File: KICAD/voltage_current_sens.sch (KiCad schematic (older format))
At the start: 14 parts, among them U10 LT6016, U11 AD8030

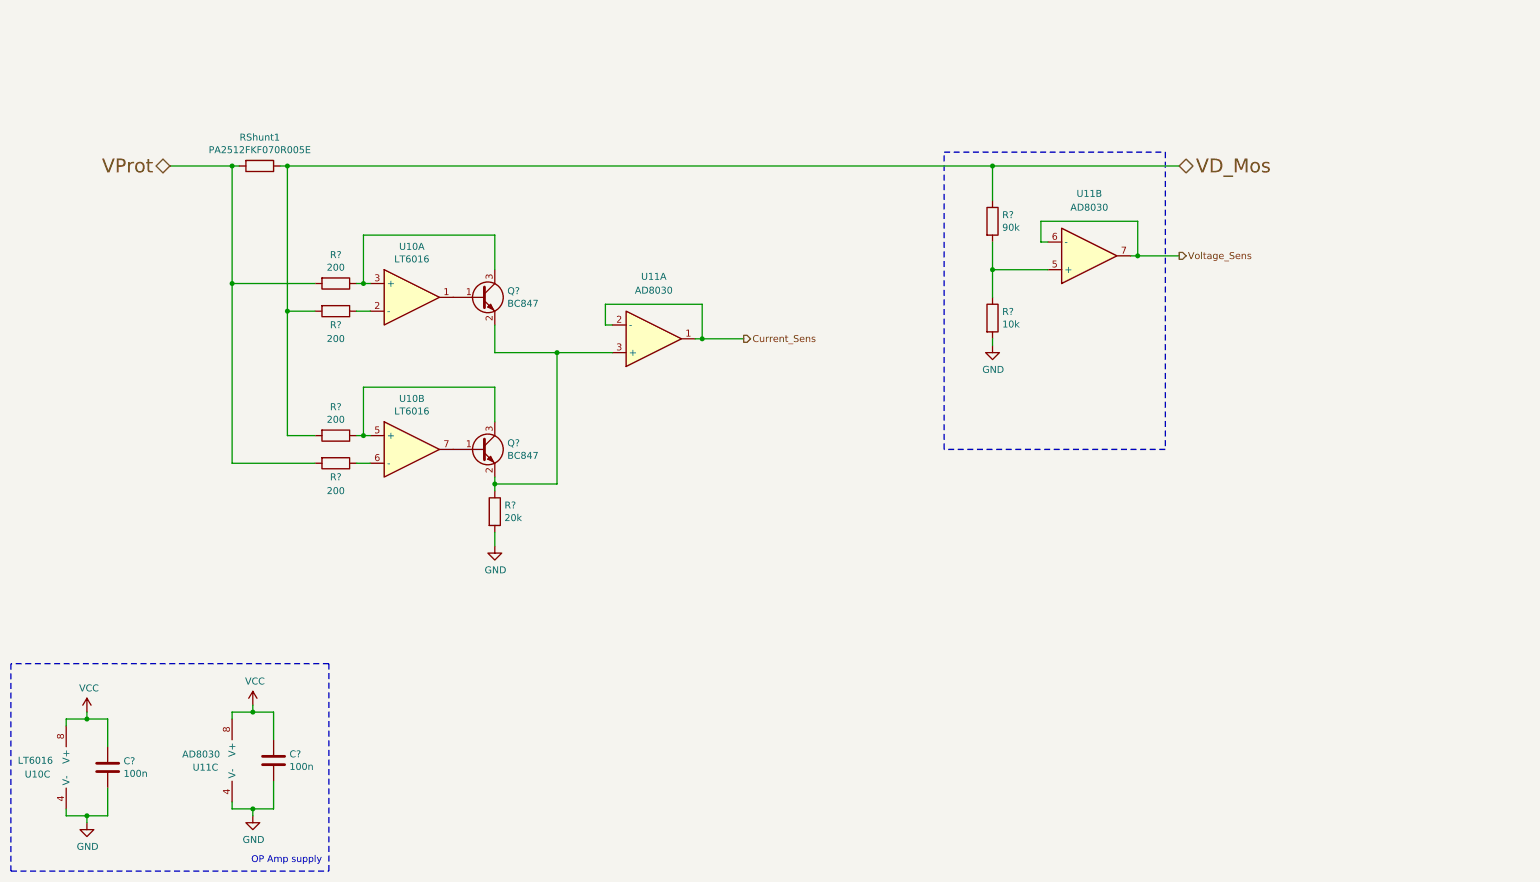
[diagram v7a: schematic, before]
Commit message: drivers draft + clean and minors changes
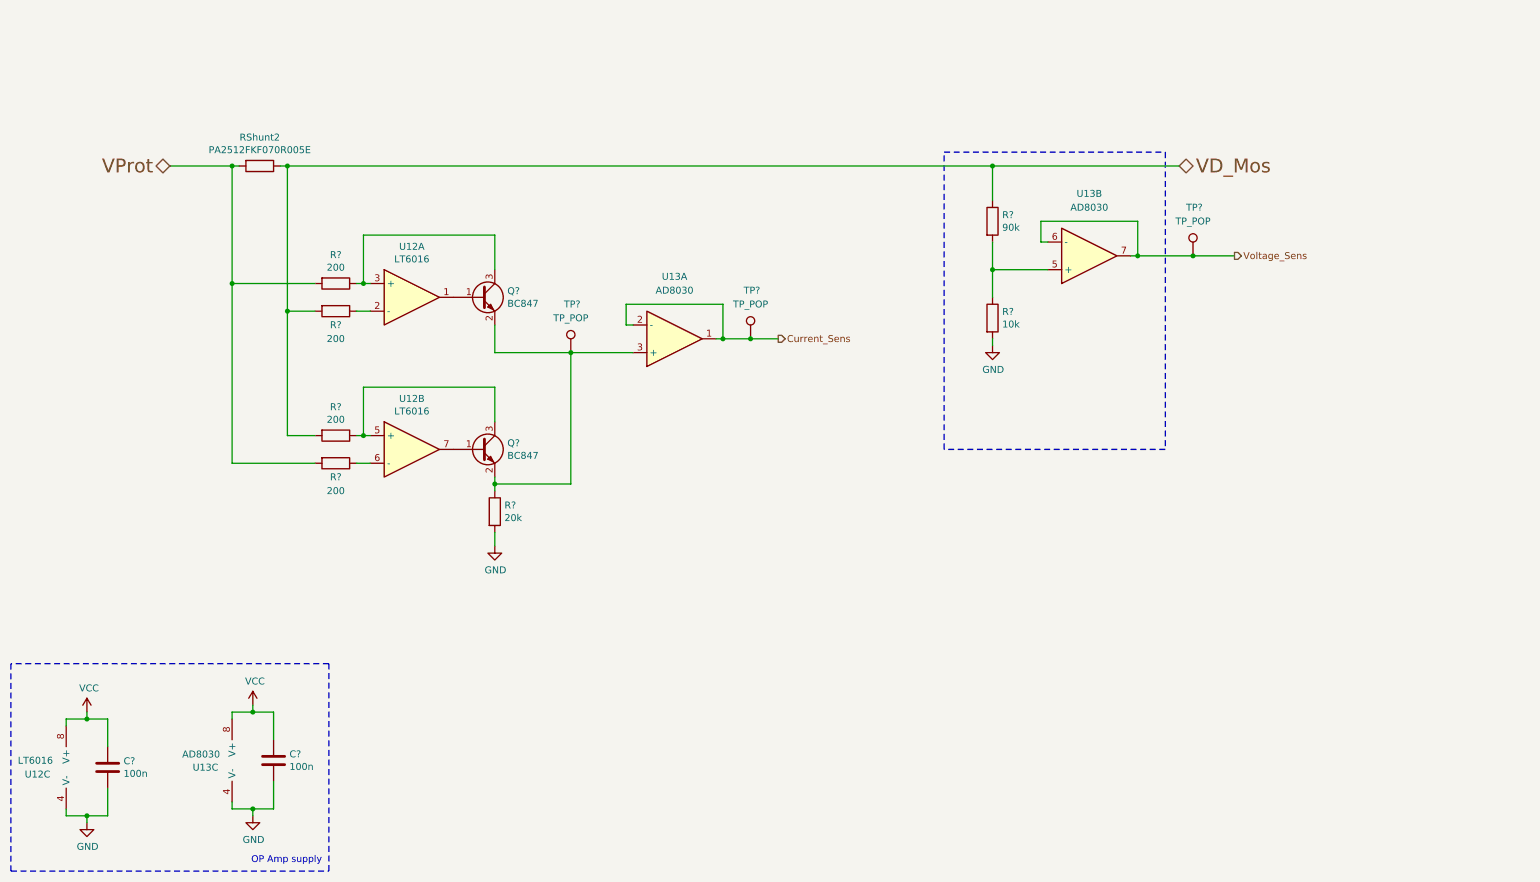
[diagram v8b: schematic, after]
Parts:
- added TP? (x3): TP_POP, symbol Connector:TestPoint
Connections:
- net Current_Sens: now also TP?.1
- net Voltage_Sens: now also TP?.1
- net at Q?.2 (E), Q?.2 (E), R?.1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: now also TP?.1
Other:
- moved on the sheet: U13A
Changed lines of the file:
@@
 $Descr A4 11693 8268
 encoding utf-8
-Sheet 8 16
+Sheet 11 16
 Title "SESAME"
 Date ""
@@
 AR Path="/60F19D5B/6109114F" Ref="RShunt2"  Part="1"
 AR Path="/60F171CE/6109114F" Ref="RShunt1"  Part="1"
-F 0 "RShunt1" V 2143 2600 50  0000 C CNN
+F 0 "RShunt2" V 2143 2600 50  0000 C CNN
 F 1 "PA2512FKF070R005E" V 2234 2600 50  0000 C CNN
 F 2 "Resistor_SMD:R_2512_6332Metric_Pad1.40x3.35mm_HandSolder" V 2280 2600 50  0001 C CNN
@@
 AR Path="/60F171CE/610DEA27" Ref="#PWR0157"  Part="1"
 AR Path="/60F19D5B/610DEA27" Ref="#PWR0112"  Part="1"
-F 0 "#PWR0157" H 7650 3650 50  0001 C CNN
+F 0 "#PWR0112" H 7650 3650 50  0001 C CNN
 F 1 "GND" H 7655 3727 50  0000 C CNN
 F 2 "" H 7650 3900 50  0001 C CNN
@@
 	1    0    0    -1
 $EndComp
-Text HLabel 9000 3250 2    50   Output ~ 0
+Text HLabel 9400 3250 2    50   Output ~ 0
 Voltage_Sens
 Text HLabel 9000 2600 2    100  BiDi ~ 0
@@
 	7650 3350 7650 3550
 Wire Wire Line
-	9000 3250 8700 3250
+	9400 3250 9100 3250
 Connection ~ 8700 3250
 Wire Wire Line
@@
 	4050 4850 4050 4900
 Wire Wire Line
-	4050 4900 4500 4900
-Wire Wire Line
-	4500 4900 4500 3950
-Wire Wire Line
-	4500 3950 4050 3950
+	4050 4900 4600 4900
+Wire Wire Line
+	4600 4900 4600 3950
+Wire Wire Line
+	4600 3950 4050 3950
 Wire Wire Line
 	4050 3950 4050 3750
@@
 AR Path="/60F171CE/6139E98B" Ref="U11"  Part="2"
 AR Path="/60F19D5B/6139E98B" Ref="U13"  Part="2"
-F 0 "U11" H 8350 2800 50  0000 C CNN
+F 0 "U13" H 8350 2800 50  0000 C CNN
 F 1 "AD8030" H 8350 2900 50  0000 C CNN
 F 2 "Package_SO:SO-8_3.9x4.9mm_P1.27mm" H 8350 3250 50  0001 C CNN
@@
 $EndComp
 Wire Wire Line
-	5500 3850 5550 3850
-Wire Wire Line
-	5550 3600 4850 3600
-Wire Wire Line
-	4850 3600 4850 3750
-Wire Wire Line
-	4850 3750 4900 3750
-Wire Wire Line
-	5550 3600 5550 3850
-Wire Wire Line
-	4900 3950 4500 3950
-Wire Wire Line
-	5850 3850 5550 3850
-Connection ~ 5550 3850
+	5650 3850 5700 3850
+Wire Wire Line
+	5700 3600 5000 3600
+Wire Wire Line
+	5000 3600 5000 3750
+Wire Wire Line
+	5000 3750 5050 3750
+Wire Wire Line
+	5700 3600 5700 3850
+Wire Wire Line
+	5050 3950 4600 3950
+Wire Wire Line
+	6100 3850 5900 3850
+Connection ~ 5700 3850
 $Comp
 L Sesame:AD8030 U11
 U 1 1 613A5251
-P 5200 3850
+P 5350 3850
 AR Path="/60F171CE/613A5251" Ref="U11"  Part="1"
 AR Path="/60F19D5B/613A5251" Ref="U13"  Part="1"
-F 0 "U11" H 5200 3400 50  0000 C CNN
-F 1 "AD8030" H 5200 3500 50  0000 C CNN
-F 2 "Package_SO:SO-8_3.9x4.9mm_P1.27mm" H 5200 3850 50  0001 C CNN
-F 3 "~" H 5200 3850 50  0001 C CNN
-	1    5200 3850
+F 0 "U13" H 5350 3400 50  0000 C CNN
+F 1 "AD8030" H 5350 3500 50  0000 C CNN
+F 2 "Package_SO:SO-8_3.9x4.9mm_P1.27mm" H 5350 3850 50  0001 C CNN
+F 3 "~" H 5350 3850 50  0001 C CNN
+	1    5350 3850
 	1    0    0    1
 $EndComp
-Connection ~ 4500 3950
-Text HLabel 5850 3850 2    50   Output ~ 0
+Connection ~ 4600 3950
+Text HLabel 6100 3850 2    50   Output ~ 0
 Current_Sens
 $Comp
@@
 AR Path="/60F171CE/613B75A3" Ref="U11"  Part="3"
 AR Path="/60F19D5B/613B75A3" Ref="U13"  Part="3"
-F 0 "U11" H 2050 6850 50  0000 R CNN
+F 0 "U13" H 2050 6850 50  0000 R CNN
 F 1 "AD8030" H 2063 6945 50  0000 R CNN
 F 2 "Package_SO:SO-8_3.9x4.9mm_P1.27mm" H 2250 6900 50  0001 C CNN
@@
 AR Path="/60F171CE/615B8C9F" Ref="U10"  Part="1"
 AR Path="/60F19D5B/615B8C9F" Ref="U12"  Part="1"
-F 0 "U10" H 3450 3917 50  0000 C CNN
+F 0 "U12" H 3450 3917 50  0000 C CNN
 F 1 "LT6016" H 3450 3826 50  0000 C CNN
 F 2 "Package_SO:MSOP-8_3x3mm_P0.65mm" H 3450 3550 50  0001 C CNN
@@
 AR Path="/60F171CE/615BC62A" Ref="U10"  Part="2"
 AR Path="/60F19D5B/615BC62A" Ref="U12"  Part="2"
-F 0 "U10" H 3450 5017 50  0000 C CNN
+F 0 "U12" H 3450 5017 50  0000 C CNN
 F 1 "LT6016" H 3450 4926 50  0000 C CNN
 F 2 "Package_SO:MSOP-8_3x3mm_P0.65mm" H 3450 4650 50  0001 C CNN
@@
 AR Path="/60F171CE/615BFCFC" Ref="U10"  Part="3"
 AR Path="/60F19D5B/615BFCFC" Ref="U12"  Part="3"
-F 0 "U10" H 650 6900 50  0000 L CNN
+F 0 "U12" H 650 6900 50  0000 L CNN
 F 1 "LT6016" H 600 7000 50  0000 L CNN
 F 2 "Package_SO:MSOP-8_3x3mm_P0.65mm" H 1050 6950 50  0001 C CNN
@@
 Wire Notes Line
 	550  7700 2850 7700
+$Comp
+L Connector:TestPoint TP?
+U 1 1 6153C862
+P 4600 3950
+AR Path="/614794AE/6153C862" Ref="TP?"  Part="1"
+AR Path="/61456C6A/6153C862" Ref="TP?"  Part="1"
+AR Path="/6153C862" Ref="TP?"  Part="1"
+AR Path="/60F1AA92/6153C862" Ref="TP?"  Part="1"
+AR Path="/60F171CE/6153C862" Ref="TP?"  Part="1"
+AR Path="/60F19D5B/6153C862" Ref="TP?"  Part="1"
+F 0 "TP?" H 4550 4300 50  0000 L CNN
+F 1 "TP_POP" H 4600 4200 50  0000 C CNN
+F 2 "" H 4800 3950 50  0001 C CNN
+F 3 "~" H 4800 3950 50  0001 C CNN
+	1    4600 3950
+	1    0    0    -1
+$EndComp
+$Comp
+L Connector:TestPoint TP?
+U 1 1 61544B27
+P 9100 3250
+AR Path="/614794AE/61544B27" Ref="TP?"  Part="1"
+AR Path="/61456C6A/61544B27" Ref="TP?"  Part="1"
+AR Path="/61544B27" Ref="TP?"  Part="1"
+AR Path="/60F1AA92/61544B27" Ref="TP?"  Part="1"
+AR Path="/60F171CE/61544B27" Ref="TP?"  Part="1"
+AR Path="/60F19D5B/61544B27" Ref="TP?"  Part="1"
+F 0 "TP?" H 9050 3600 50  0000 L CNN
+F 1 "TP_POP" H 9100 3500 50  0000 C CNN
+F 2 "" H 9300 3250 50  0001 C CNN
+F 3 "~" H 9300 3250 50  0001 C CNN
+	1    9100 3250
+	1    0    0    -1
+$EndComp
+Connection ~ 9100 3250
+Wire Wire Line
+	9100 3250 8700 3250
+$Comp
+L Connector:TestPoint TP?
+U 1 1 6154A16C
+P 5900 3850
+AR Path="/614794AE/6154A16C" Ref="TP?"  Part="1"
+AR Path="/61456C6A/6154A16C" Ref="TP?"  Part="1"
+AR Path="/6154A16C" Ref="TP?"  Part="1"
+AR Path="/60F1AA92/6154A16C" Ref="TP?"  Part="1"
+AR Path="/60F171CE/6154A16C" Ref="TP?"  Part="1"
+AR Path="/60F19D5B/6154A16C" Ref="TP?"  Part="1"
+F 0 "TP?" H 5850 4200 50  0000 L CNN
+F 1 "TP_POP" H 5900 4100 50  0000 C CNN
+F 2 "" H 6100 3850 50  0001 C CNN
+F 3 "~" H 6100 3850 50  0001 C CNN
+	1    5900 3850
+	1    0    0    -1
+$EndComp
+Connection ~ 5900 3850
+Wire Wire Line
+	5900 3850 5700 3850
 $EndSCHEMATC
